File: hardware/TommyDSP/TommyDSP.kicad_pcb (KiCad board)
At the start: 2 copper layers, 85 x 85 mm, 148 parts, among them J401 Conn_01x02_Pin, J501 USB_C_Receptacle_USB2.0_16P, J502 AudioJack3_SwitchTR, J503 XH-2.50mm Horizontal, J504 AudioJack3_SwitchTR, J505 EXT.IN, J506 AudioJack3_SwitchTR, J507 XH-2.50mm Horizontal, J508 EXT.OUT, J509 Conn_01x03_Pin, J510 AudioJack3_SwitchTR, J511 Micro_SD_Card_Det1, J512 Qwiic, Q401 AO3401A, SW201 SW_Push, SW202 SW_Push, SW501 RotaryEncoder_Switch_MP, U201 W25Q128JVS, U202 DNF, U203 RP2350_60QFN, U301 ES8388/WM8988, U401 TPS7A2033PDBVR, U402 TPS62A01APDDC, U403 TP4056-42-ESOP8, Y201 ABM8-272-T3

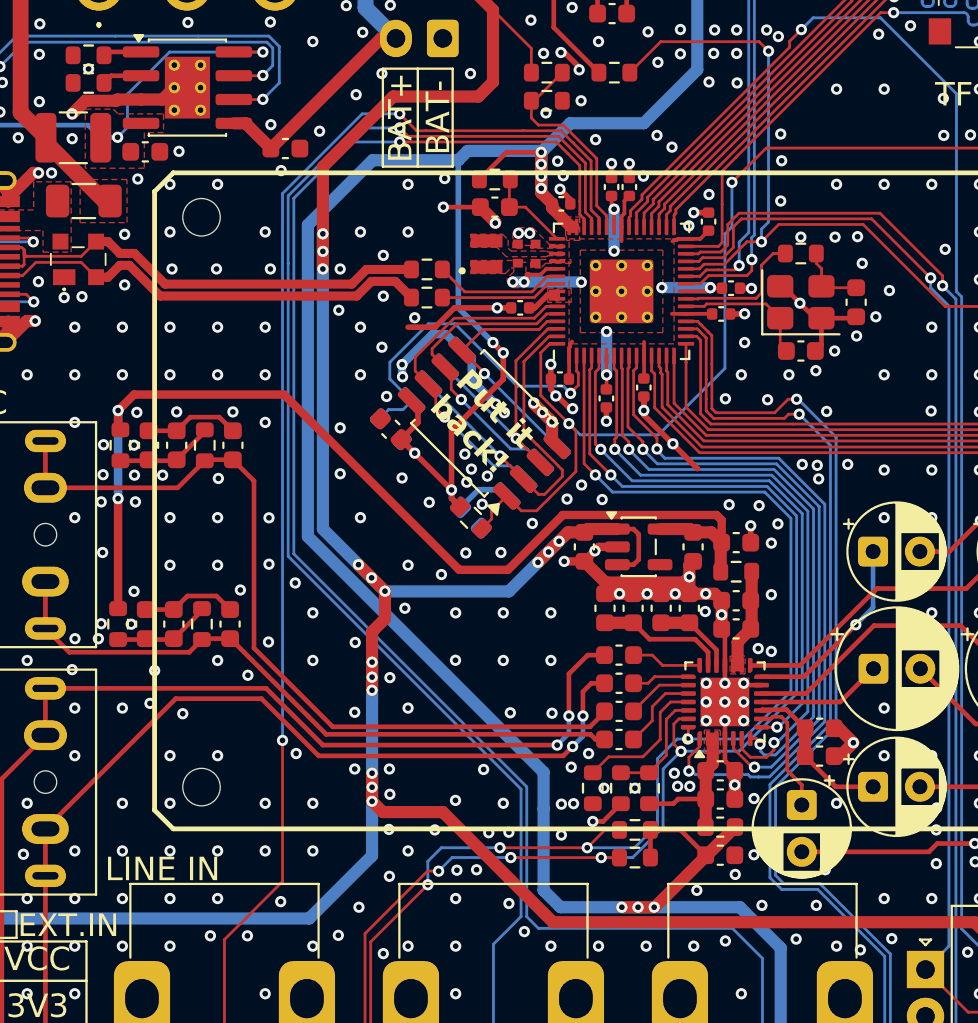
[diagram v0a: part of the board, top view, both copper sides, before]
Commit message: hardware: add PAM8406 audio amplifier board
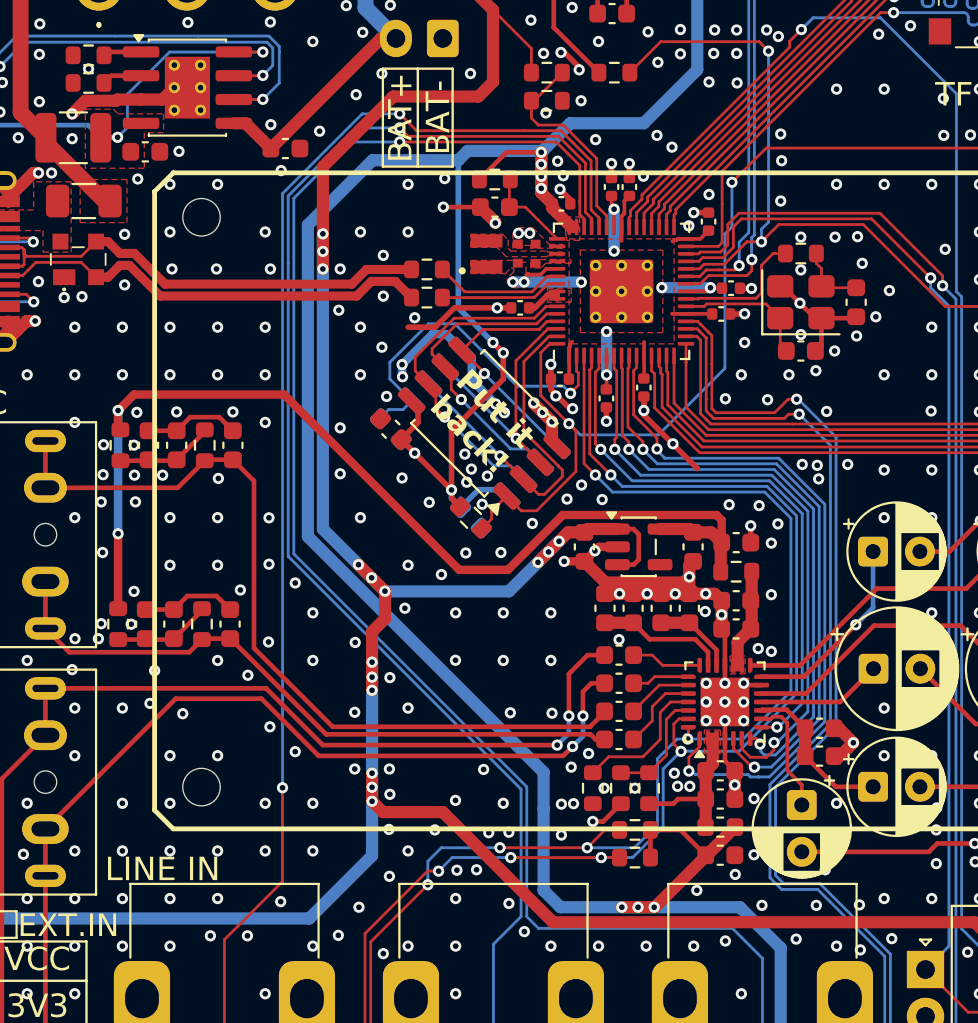
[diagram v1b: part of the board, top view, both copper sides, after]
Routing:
- net GND: vias 820 -> 825

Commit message: hardware: minor tweaks
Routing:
- net GND: track 111.3 -> 109.9 mm, vias 825 -> 888
- net Net-(D401-A): track 27.3 -> 28.4 mm
- net /ROTARY_ENCODER_BUTTON: track 85.7 -> 84.8 mm
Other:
- board text added: "Jason Chen 2026.02 REV 1.0.0"
- board text added: "TommyDSP"
- board text removed: "Jason Chen 2026.02"
- board text removed: "TommyDSP REV 1.0.0"

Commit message: hardware: add misc project files
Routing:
- net GND: track 109.9 -> 131.8 mm, vias 888 -> 1037
- net /MCU-Core/QSPI_SS: track 63.2 -> 59.9 mm, vias 2 -> 4
- net +3.3VA: track 55.8 -> 56.3 mm
- net /MCU-Core/GPIO0: track 18.9 -> 19.4 mm
